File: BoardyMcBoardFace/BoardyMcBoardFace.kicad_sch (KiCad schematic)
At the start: 92 parts, among them J1 SMA, J2 ARM 10pin, J3 USB_B_Micro, SW1 SW_Push, U1 nRF24L01P, U2 STM32F103CBT6, U3 USBLC6-2SC6, U4 LM393, U5 AMS1117-5.0, U6 AMS1117-3.3, U7 USBLC6-2SC6, U8 USBLC6-2SC6, U9 MCP2551-I-SN, Y1 16MHz, Y2 16MHz

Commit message: wip
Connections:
- net GND: no longer U$1.P$57 (57), U$1.P$59 (59), U$1.P$61 (61), U$1.P$63 (63), U$1.P$65 (65), U$1.P$67 (67), U$1.P$69 (69), U$1.P$71 (71), U$1.P$73 (73), U$1.P$75 (75)
- net I2C1_SCL: now also U$1.P$35 (35), U$1.P$37 (37); no longer U$1.P$3 (3), U$1.P$5 (5)
- net I2C1_SDA: now also U$1.P$39 (39), U$1.P$41 (41); no longer U$1.P$7 (7), U$1.P$9 (9)
- net PIXEL_OFFBOARD: now reaches D18.2 (DOUT)
- net PIXEL_OFFBOARD: now also U$1.P$73 (73), U$1.P$75 (75)
- net PIXEL_MISO: no longer names the net of U2.3 (PC14)
- net PIXEL_MISO: no longer U$1.P$45 (45)
- new net: U$1.P$57 (57), U$1.P$59 (59), U$1.P$61 (61), U$1.P$63 (63), U$1.P$65 (65), U$1.P$67 (67), U$1.P$69 (69), U$1.P$71 (71)
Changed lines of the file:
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@@
   (junction (at 250.19 71.755) (diameter 0) (color 0 0 0 0)
   )
+  (junction (at 400.05 207.645) (diameter 0) (color 0 0 0 0)
+  )
   (junction (at 59.055 189.23) (diameter 0) (color 0 0 0 0)
   )
@@
   (junction (at 328.295 33.655) (diameter 0) (color 0 0 0 0)
   )
-  (junction (at 265.43 71.755) (diameter 0) (color 0 0 0 0)
-  )
   (junction (at 82.55 176.53) (diameter 0) (color 0 0 0 0)
   )
@@
   (junction (at 52.07 203.2) (diameter 0) (color 0 0 0 0)
   )
-  (junction (at 262.89 71.755) (diameter 0) (color 0 0 0 0)
-  )
   (junction (at 124.46 20.955) (diameter 0) (color 0 0 0 0)
   )
@@
   (junction (at 201.93 245.745) (diameter 0) (color 0 0 0 0)
   )
+  (junction (at 389.89 212.725) (diameter 0) (color 0 0 0 0)
+  )
   (junction (at 57.785 134.62) (diameter 0) (color 0 0 0 0)
   )
@@
   )
   (junction (at 59.055 176.53) (diameter 0) (color 0 0 0 0)
-  )
-  (junction (at 260.35 71.755) (diameter 0) (color 0 0 0 0)
   )
   (no_connect (at 327.66 67.31))
   (no_connect (at 72.39 235.585))
+  (no_connect (at 387.858 212.725))
   (no_connect (at 245.11 97.155))
-  (no_connect (at 389.89 212.725))
   (no_connect (at 394.335 130.81))
-  (no_connect (at 400.05 207.645))
   (no_connect (at 381.635 130.81))
-  (no_connect (at 287.655 238.125))
   (no_connect (at 173.99 84.455))
   (no_connect (at 194.31 71.755))
+  (no_connect (at 402.336 205.232))
+  (no_connect (at 72.39 68.58))
   (no_connect (at 181.61 71.755))
   (no_connect (at 201.93 71.755))
@@
     (stroke (width 0) (type default) (color 0 0 0 0))
   )
-  (wire (pts (xy 265.43 69.215) (xy 265.43 71.755))
-    (stroke (width 0) (type default) (color 0 0 0 0))
-  )
   (polyline (pts (xy 311.785 187.325) (xy 311.785 150.495))
     (stroke (width 0) (type default) (color 0 0 0 0))
@@
     (stroke (width 0) (type default) (color 0 0 0 0))
   )
-  (wire (pts (xy 260.35 71.755) (xy 262.89 71.755))
-    (stroke (width 0) (type default) (color 0 0 0 0))
-  )
   (wire (pts (xy 64.77 153.67) (xy 57.785 153.67))
     (stroke (width 0) (type default) (color 0 0 0 0))
@@
     (stroke (width 0) (type default) (color 0 0 0 0))
   )
-  (wire (pts (xy 262.89 71.755) (xy 265.43 71.755))
-    (stroke (width 0) (type default) (color 0 0 0 0))
-  )
   (wire (pts (xy 48.26 107.315) (xy 48.26 103.505))
     (stroke (width 0) (type default) (color 0 0 0 0))
@@
     (stroke (width 0) (type default) (color 0 0 0 0))
   )
+  (wire (pts (xy 389.89 212.725) (xy 390.017 212.725))
+    (stroke (width 0) (type default) (color 0 0 0 0))
+  )
   (wire (pts (xy 156.21 245.745) (xy 171.45 245.745))
     (stroke (width 0) (type default) (color 0 0 0 0))
@@
     (stroke (width 0) (type default) (color 0 0 0 0))
   )
+  (wire (pts (xy 400.05 207.645) (xy 400.05 205.232))
+    (stroke (width 0) (type default) (color 0 0 0 0))
+  )
   (wire (pts (xy 325.12 77.47) (xy 327.66 77.47))
     (stroke (width 0) (type default) (color 0 0 0 0))
@@
     (stroke (width 0) (type default) (color 0 0 0 0))
   )
+  (wire (pts (xy 387.858 212.725) (xy 389.89 212.725))
+    (stroke (width 0) (type default) (color 0 0 0 0))
+  )
   (wire (pts (xy 29.21 191.77) (xy 36.83 191.77))
     (stroke (width 0) (type default) (color 0 0 0 0))
@@
     (stroke (width 0) (type default) (color 0 0 0 0))
   )
+  (wire (pts (xy 400.05 205.232) (xy 402.336 205.232))
+    (stroke (width 0) (type default) (color 0 0 0 0))
+  )
   (wire (pts (xy 390.525 29.845) (xy 393.7 29.845))
     (stroke (width 0) (type default) (color 0 0 0 0))
   )
   (wire (pts (xy 222.25 97.155) (xy 224.79 97.155))
+    (stroke (width 0) (type default) (color 0 0 0 0))
+  )
+  (wire (pts (xy 400.05 207.772) (xy 400.05 207.645))
     (stroke (width 0) (type default) (color 0 0 0 0))
   )
@@
     (effects (font (size 1.27 1.27)) (justify left bottom))
   )
-  (label "I2C1_SCL" (at 184.15 71.755 90)
+  (label "I2C1_SCL" (at 214.63 71.755 90)
     (effects (font (size 1.27 1.27)) (justify left bottom))
   )
@@
     (effects (font (size 1.27 1.27)) (justify left bottom))
   )
-  (label "I2C1_SDA" (at 191.77 71.755 90)
+  (label "I2C1_SDA" (at 222.25 71.755 90)
     (effects (font (size 1.27 1.27)) (justify left bottom))
   )
@@
     (effects (font (size 1.27 1.27)) (justify right bottom))
   )
-  (label "PIXEL_MISO" (at 72.39 68.58 0)
-    (effects (font (size 1.27 1.27)) (justify left bottom))
-  )
   (label "PB15" (at 72.39 114.3 0)
+    (effects (font (size 1.27 1.27)) (justify left bottom))
+  )
+  (label "PIXEL_OFFBOARD" (at 265.43 71.755 90)
     (effects (font (size 1.27 1.27)) (justify left bottom))
   )
@@
     (effects (font (size 1.27 1.27)) (justify right bottom))
   )
-  (label "PIXEL_MISO" (at 227.33 71.755 90)
-    (effects (font (size 1.27 1.27)) (justify left bottom))
-  )
   (label "SWCLK_CONN" (at 396.24 125.73 0)
     (effects (font (size 1.27 1.27)) (justify left bottom))
@@
     (effects (font (size 1.27 1.27)) (justify right bottom))
   )
+  (label "PIXEL_OFFBOARD" (at 262.89 71.755 90)
+    (effects (font (size 1.27 1.27)) (justify left bottom))
+  )
   (label "PA10" (at 135.89 101.6 180)
     (effects (font (size 1.27 1.27)) (justify right bottom))
@@
     (effects (font (size 1.27 1.27)) (justify right bottom))
   )
-  (label "I2C1_SCL" (at 186.69 71.755 90)
+  (label "PIXEL_OFFBOARD" (at 287.655 238.125 0)
+    (effects (font (size 1.27 1.27)) (justify left bottom))
+  )
+  (label "I2C1_SCL" (at 217.17 71.755 90)
     (effects (font (size 1.27 1.27)) (justify left bottom))
   )
@@
     (effects (font (size 1.27 1.27)) (justify right bottom))
   )
-  (label "I2C1_SDA" (at 189.23 71.755 90)
+  (label "I2C1_SDA" (at 219.71 71.755 90)
     (effects (font (size 1.27 1.27)) (justify left bottom))
   )
@@
     (effects (font (size 1.27 1.27)) (justify left bottom))
   )
-  (label "GND" (at 265.43 69.215 90)
-    (effects (font (size 1.27 1.27)) (justify left bottom))
-  )
+  (label "GND" (at 257.81 71.628 90)
+    (effects (font (size 1.27 1.27)) (justify left bottom))
+  )

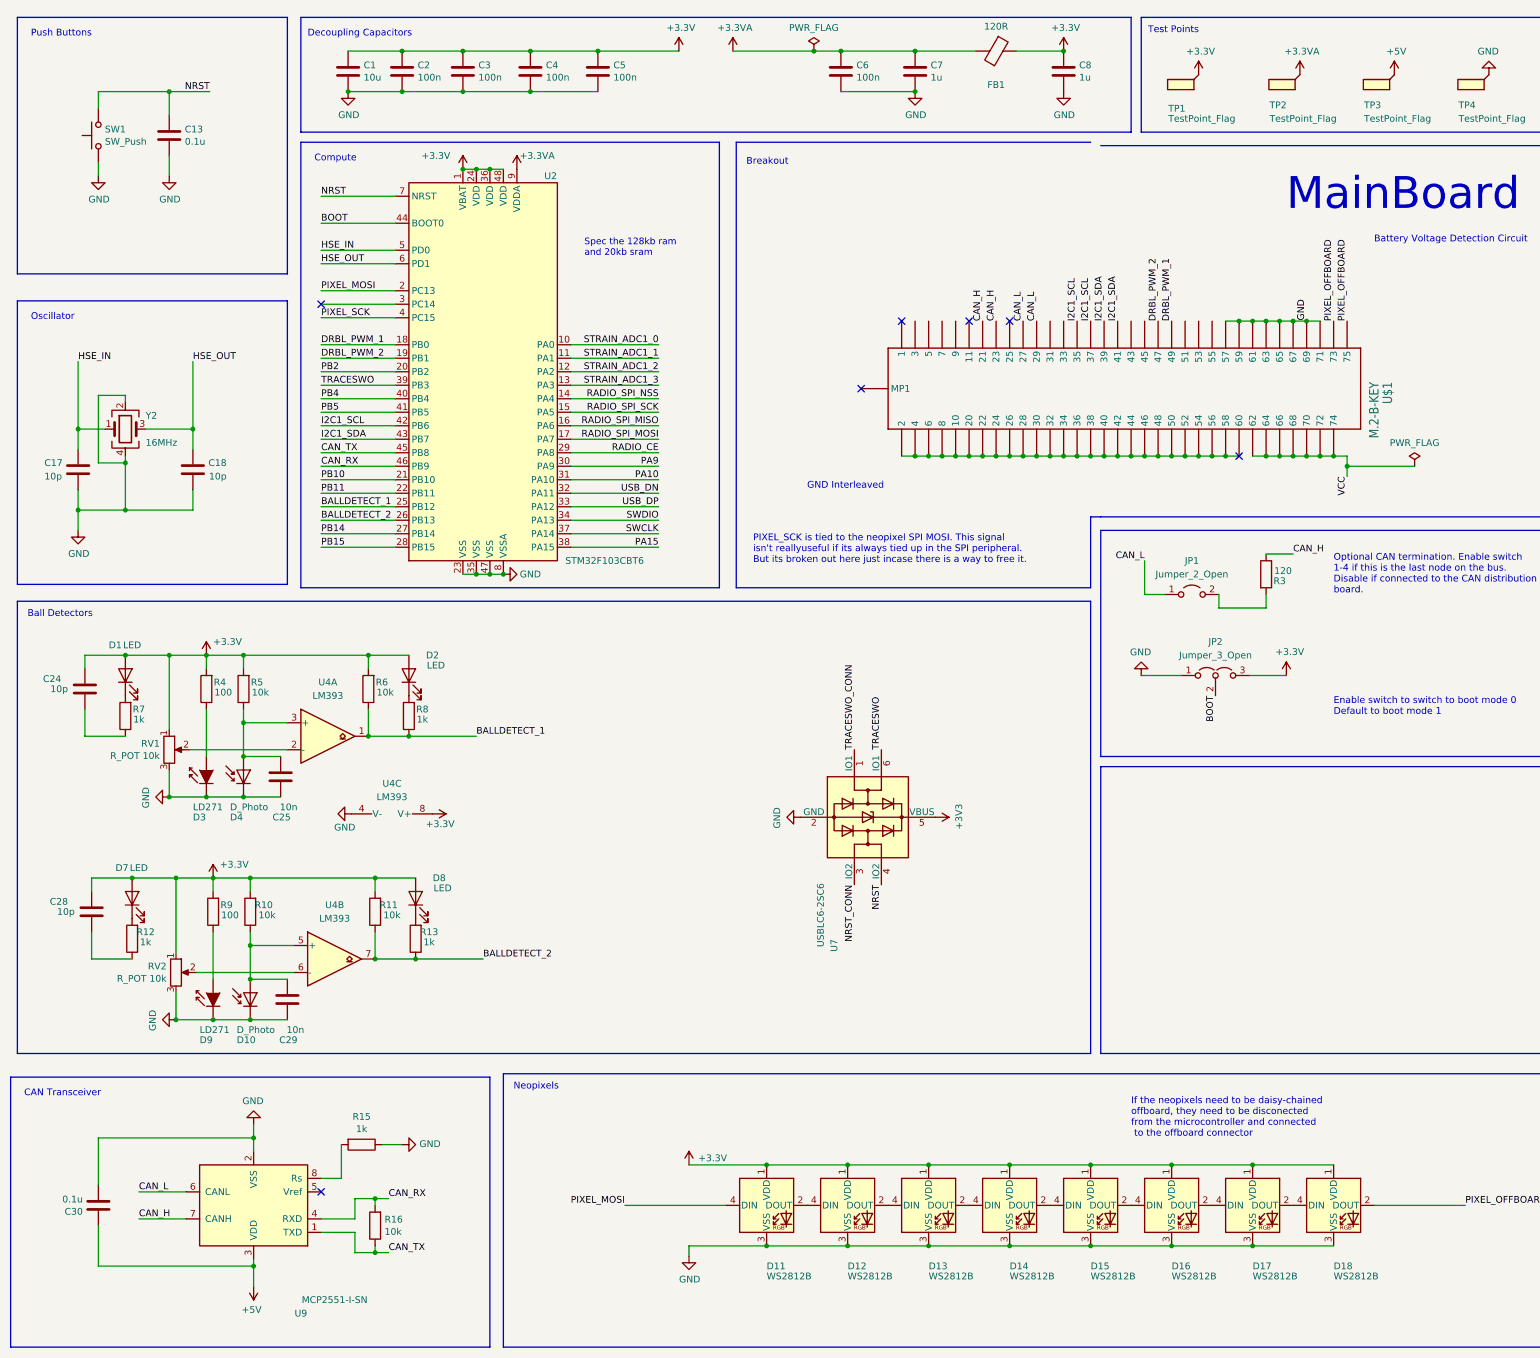
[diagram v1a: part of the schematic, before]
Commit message: most DRC stuff fixed
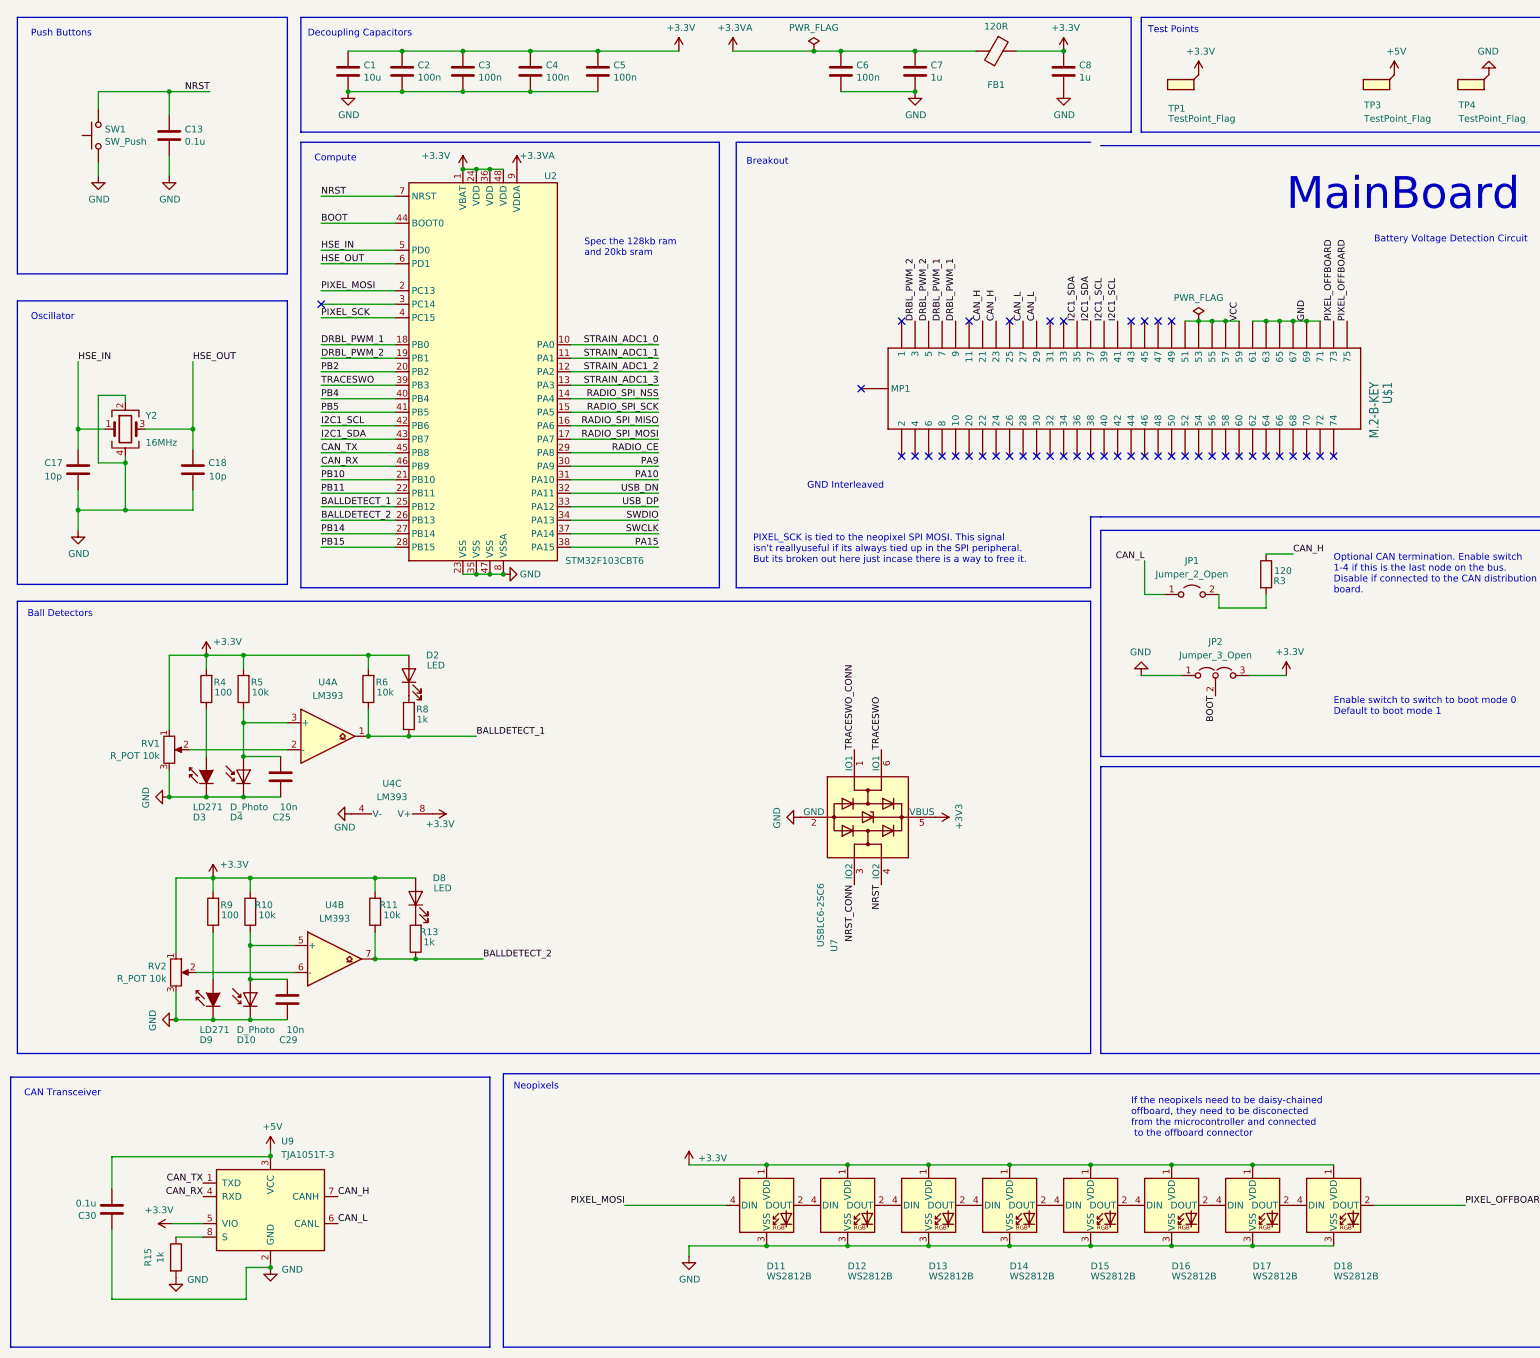
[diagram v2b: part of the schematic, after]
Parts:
- removed C24, C28: 10p, Capacitor_SMD:C_0402_1005Metric, symbol Device:C
- removed D1, D7: LED, LED_SMD:LED_0402_1005Metric, symbol Device:LED
- removed R12, R7: 1k, Resistor_SMD:R_0402_1005Metric, symbol Device:R
- removed R16: 10k, Resistor_SMD:R_0402_1005Metric, symbol Device:R
- removed TP2: TestPoint_Flag, TestPoint:TestPoint_Pad_1.0x1.0mm, symbol Connector:TestPoint_Flag
- removed U9: MCP2551-I-SN, Package_SO:SOIC-8_3.9x4.9mm_P1.27mm, symbol Interface_CAN_LIN:MCP2551-I-SN
- added U9: TJA1051T-3, Package_SO:SOIC-8_3.9x4.9mm_P1.27mm, symbol Interface_CAN_LIN:TJA1051T-3
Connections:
- net +3V3: now also U9.5 (VIO)
- net +5V: now also C30.2, U9.3 (VCC); no longer C30.1
- net CAN_H: now also U9.7 (CANH)
- net CAN_L: now also U9.6 (CANL)
- net CAN_RX: now also U9.4 (RXD)
- net CAN_TX: now also U9.1 (TXD)
- net DRBL_PWM_1: now also U$1.P$7 (7), U$1.P$9 (9); no longer U$1.P$49 (49)
- net DRBL_PWM_2: now also U$1.P$3 (3), U$1.P$5 (5); no longer U$1.P$47 (47)
- net GND: now also C30.1, R15.2, U$1.P$61 (61), U$1.P$63 (63), U$1.P$65 (65), U$1.P$67 (67), U$1.P$69 (69), U$1.P$71 (71), U9.2 (GND); no longer C30.2, R15.1
- net I2C1_SCL: now also U$1.P$39 (39), U$1.P$41 (41); no longer U$1.P$35 (35), U$1.P$37 (37)
- net I2C1_SDA: now also U$1.P$35 (35), U$1.P$37 (37); no longer U$1.P$39 (39), U$1.P$41 (41)
- net VCC: now also U$1.P$51 (51), U$1.P$53 (53), U$1.P$55 (55), U$1.P$57 (57), U$1.P$59 (59); no longer U$1.P$62 (62), U$1.P$64 (64), U$1.P$66 (66), U$1.P$68 (68), U$1.P$70 (70), U$1.P$72 (72), U$1.P$74 (74)
- new net: R15.1, U9.8 (S)
- now unconnected: U$1.P$10 (10), U$1.P$2 (2), U$1.P$20 (20), U$1.P$22 (22), U$1.P$24 (24), U$1.P$26 (26), U$1.P$28 (28), U$1.P$30 (30), U$1.P$32 (32), U$1.P$34 (34), U$1.P$36 (36), U$1.P$38 (38), U$1.P$4 (4), U$1.P$40 (40), U$1.P$42 (42), U$1.P$44 (44), U$1.P$46 (46), U$1.P$48 (48), U$1.P$50 (50), U$1.P$52 (52), U$1.P$54 (54), U$1.P$56 (56), U$1.P$58 (58), U$1.P$6 (6), U$1.P$60 (60), U$1.P$8 (8)
- no-connect marks 12 -> 49
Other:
- moved on the sheet: C30, R15

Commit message: routing finished
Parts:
- removed R14: 1k5, Resistor_SMD:R_0402_1005Metric, symbol Device:R
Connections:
- net PB14 is gone; now on net RADIO_SPI_MISO: U2.27 (PB14)
- net PB15 is gone; now on net RADIO_SPI_MOSI: U2.28 (PB15)
- net BALLDETECT_1: now also U2.15 (PA5); no longer U2.25 (PB12)
- net BALLDETECT_2: now also U2.14 (PA4); no longer U2.26 (PB13)
- net CAN_H: now also U$1.P$3 (3), U$1.P$5 (5); no longer U$1.P$21 (21), U$1.P$23 (23)
- net CAN_L: now also U$1.P$7 (7), U$1.P$9 (9); no longer U$1.P$27 (27), U$1.P$29 (29)
- net DRBL_PWM_1: now also U$1.P$35 (35), U$1.P$37 (37); no longer U$1.P$7 (7), U$1.P$9 (9)
- net DRBL_PWM_2: now also U$1.P$39 (39), U$1.P$41 (41); no longer U$1.P$3 (3), U$1.P$5 (5)
- net I2C1_SCL: now also U$1.P$25 (25), U$1.P$27 (27); no longer U$1.P$39 (39), U$1.P$41 (41)
- net I2C1_SDA: now also U$1.P$21 (21), U$1.P$23 (23); no longer U$1.P$35 (35), U$1.P$37 (37)
- net PIXEL_MOSI: now also U2.17 (PA7); no longer U2.2 (PC13)
- net RADIO_SPI_MISO: no longer U2.16 (PA6)
- net RADIO_SPI_MOSI: no longer U2.17 (PA7)
- net RADIO_SPI_NSS: now also U2.25 (PB12); no longer U2.14 (PA4)
- net RADIO_SPI_SCK: now also U2.26 (PB13); no longer U2.15 (PA5)
- net PA10: no longer names the net of U2.31 (PA10)
- net PA15: no longer names the net of U2.38 (PA15)
- net PA9: no longer names the net of U2.30 (PA9)
- net PB10: no longer names the net of U2.21 (PB10)
- net PB11: no longer names the net of U2.22 (PB11)
- net PB2: no longer names the net of U2.20 (PB2)
- net PB4: no longer names the net of U2.40 (PB4)
- net PB5: no longer names the net of U2.41 (PB5)
- net PIXEL_SCK: no longer names the net of U2.4 (PC15)
- no-connect marks 49 -> 60
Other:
- note removed: "PIXEL_SCK is tied to the neopixel SPI MOSI. This signal isn't reallyuseful if its always tied up in the SPI peripheral. But its broken out here just incase there is a way to free it."
- moved on the sheet: C20, TP1, TP3, TP4, U3, U7

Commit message: wip
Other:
- moved on the sheet: C20, C25, C29, D10, D2, D3, D4, D8, D9, J2, R10, R11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

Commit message: wip
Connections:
- net GND: now also J3.6 (Shield)
- no-connect marks 60 -> 59
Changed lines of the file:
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@@
   (junction (at 257.81 71.755) (diameter 0) (color 0 0 0 0)
+  )
+  (junction (at 397.51 207.645) (diameter 0) (color 0 0 0 0)
   )
   (junction (at 347.345 24.765) (diameter 0) (color 0 0 0 0)
@@
   (no_connect (at 181.61 71.755))
   (no_connect (at 72.39 104.14))
-  (no_connect (at 400.05 207.645))
   (no_connect (at 217.17 97.155))
   (no_connect (at 135.89 99.06))
@@
     (stroke (width 0) (type default) (color 0 0 0 0))
   )
+  (wire (pts (xy 397.51 207.645) (xy 400.05 207.645))
+    (stroke (width 0) (type default) (color 0 0 0 0))
+  )
